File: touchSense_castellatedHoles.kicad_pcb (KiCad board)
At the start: 2 copper layers, 15 x 10 mm, 10 parts, among them J1 breakout, J2 GS2, U1 AT42QT1010-TSHR

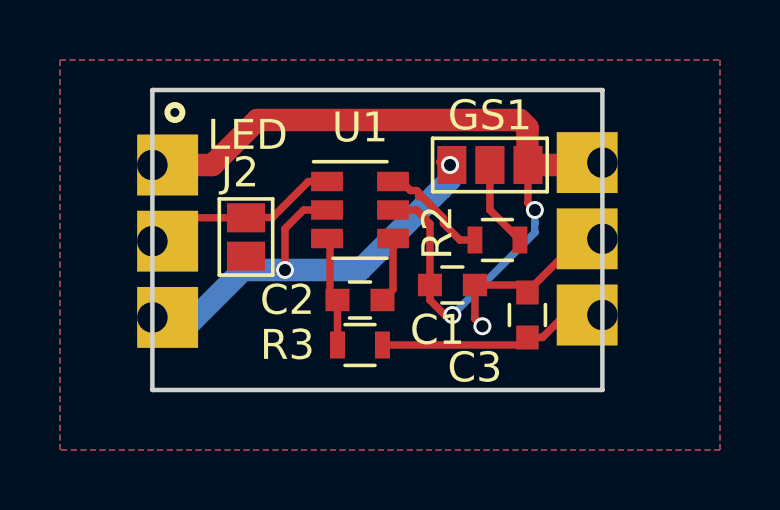
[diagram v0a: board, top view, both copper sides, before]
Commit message: new touch implementation
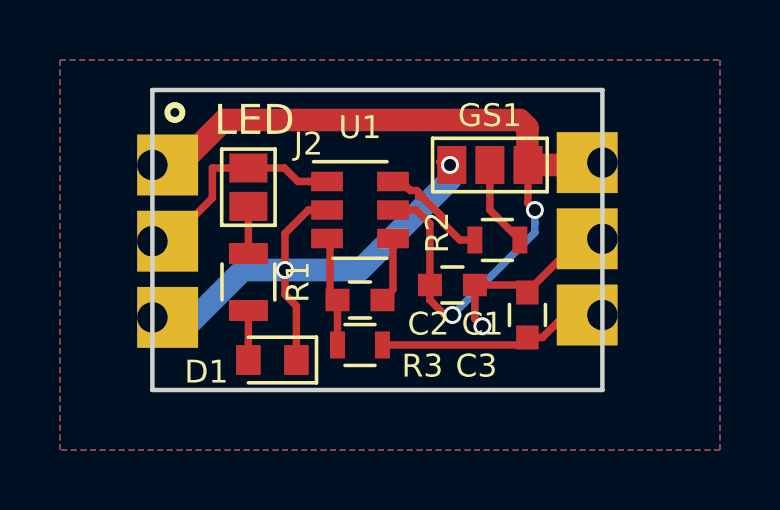
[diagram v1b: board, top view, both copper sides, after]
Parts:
- added D1: LED_0603_1608Metric, LED_SMD:LED_0603_1608Metric, F.Cu at (109.1, 109.0)
- added R1: R_0805, Resistors_SMD:R_0805, F.Cu at (108.3, 106.4)
- moved J2 1.66 mm to (108.3, 103.2)
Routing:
- net GND: track 22.3 -> 25.4 mm
- net /OUT1: track 8.04 -> 10.4 mm
- net (no net): track 0.00 -> 1.65 mm
- net Net-(D1-Pad2): track 0.36 -> 1.93 mm

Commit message: organize project folder, small pcb maitenance, generated gerbers
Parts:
- U1: value AT42QT1010-TSHR -> VDFN-8-1EP_2x2mm_Pitch0.5mm; footprint TO_SOT_Packages_SMD:SOT-23-6 -> Housings_DFN_QFN:VDFN-8-1EP_2x2mm_Pitch0.5mm
- moved R2 0.72 mm to (116.0, 104.6)
- moved U1 0.51 mm to (112.1, 103.5), turned to 180 degrees
- moved GS1 0.30 mm to (116.3, 102.2)
- moved C2 0.08 mm to (112.1, 107.0), turned to 180 degrees
- renumbered J2 to GS2
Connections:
- U1 pad 1: /OUT1 -> Net-(C2-Pad1)
- U1 pad 2: GND -> (no net)
- U1 pad 3: Net-(C2-Pad1) -> (no net)
- U1 pad 4: Net-(C2-Pad2) -> GND
- U1 pad 5: /VDD -> /OUT1
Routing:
- net /VDD: track 28.8 -> 35.1 mm, vias 2 -> 3
- net Net-(R2-Pad2): track 3.73 -> 7.86 mm, vias 0 -> 2
- net /OUT1: track 10.4 -> 8.08 mm
- net Net-(C2-Pad1): track 3.69 -> 5.17 mm
- net GND: track 25.4 -> 24.2 mm
- net Net-(C2-Pad2): track 2.19 -> 2.85 mm
